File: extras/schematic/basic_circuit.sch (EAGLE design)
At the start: 11 parts, among them M1 ARDUINO-PRO-MINI-3.3V, Y1 32.768kHz

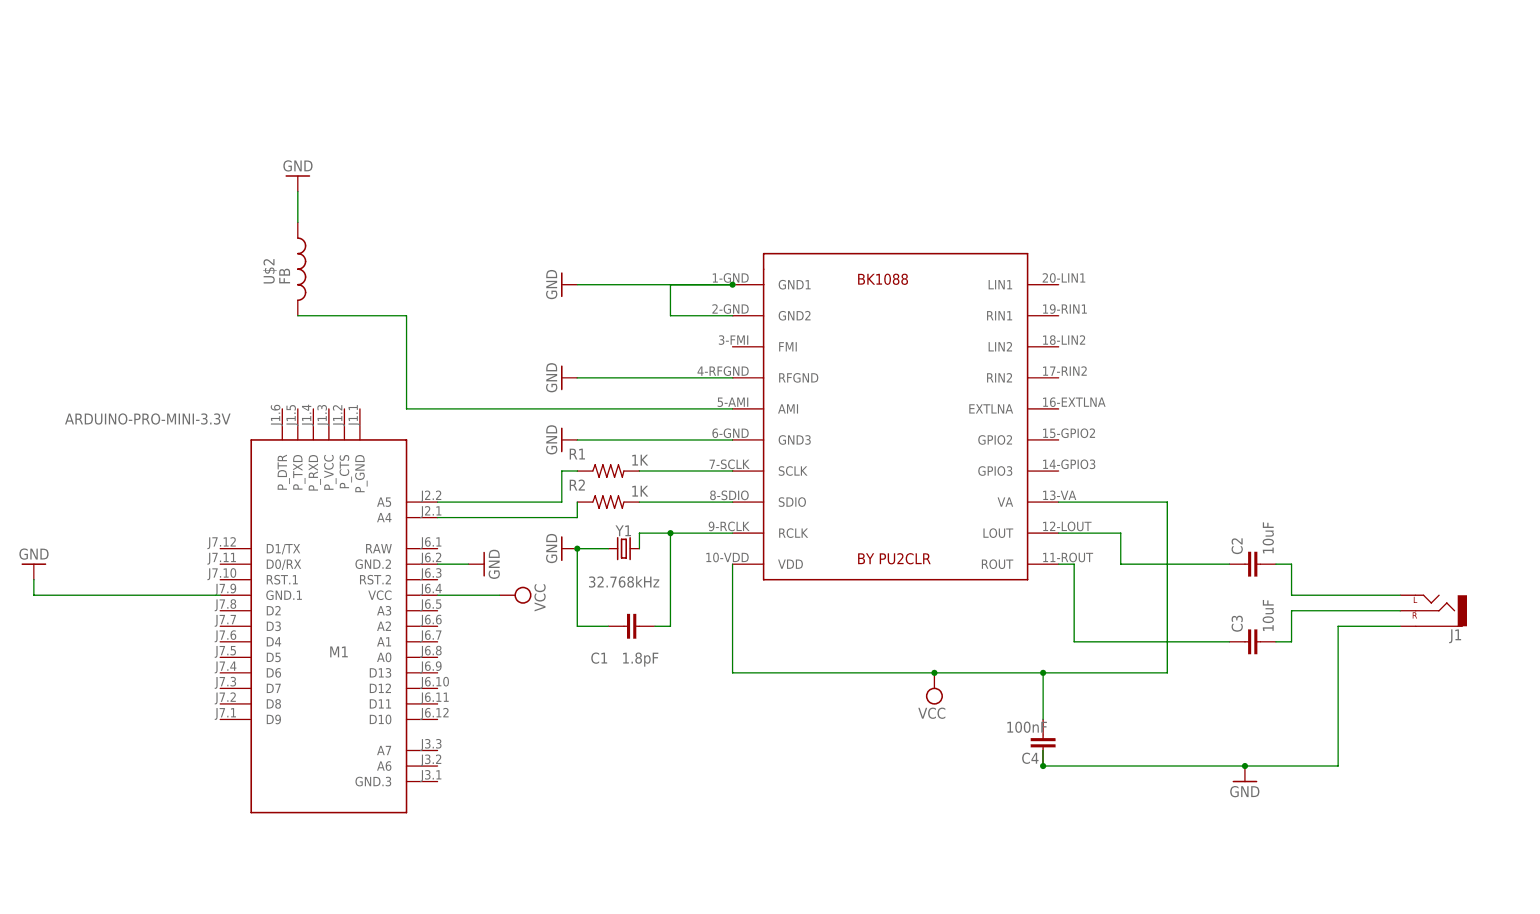
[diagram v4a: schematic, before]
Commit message: BK1088 Arduino Library
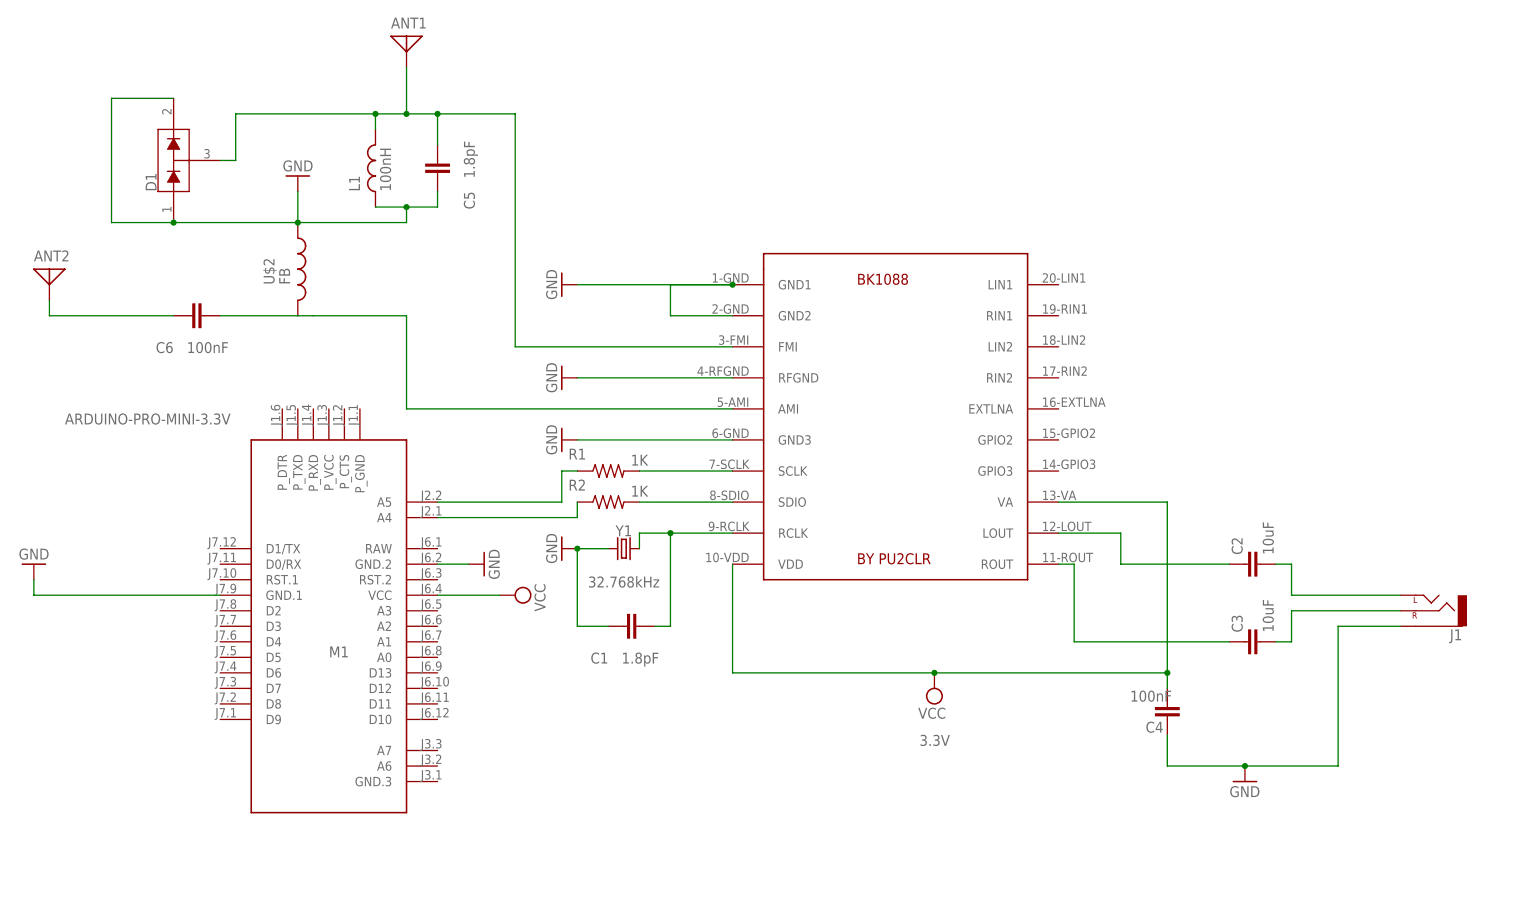
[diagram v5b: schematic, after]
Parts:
- added ANT1, ANT2: (no value), discrete:ANTENNA
- added C5: 1.8pF, capacitor-wima:C5/3
- added C6: 100nF, capacitor-wima:C5/3
- added D1: 200mA/70V, SparkFun-DiscreteSemi:BAV99
- added L1: 100nH, ngspice-simulation:L
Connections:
- new net N$11: ANT2.1, C6.1
- new net N$12: ANT1.1, C5.2, D1.COM, L1.2, U$1.FMI
- net GND: now also C5.1, D1.A1, D1.C2, L1.1
- net N$10: now also C6.2
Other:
- moved on the sheet: C4
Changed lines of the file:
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@@
 <part name="R1" library="Resistor" library_urn="urn:adsk.eagle:library:16378527" deviceset="R-US" device="AXIAL-7.2MM-PITCH" package3d_urn="urn:adsk.eagle:package:16378561/2" technology="_" value="1K"/>
 <part name="R2" library="Resistor" library_urn="urn:adsk.eagle:library:16378527" deviceset="R-US" device="AXIAL-7.2MM-PITCH" package3d_urn="urn:adsk.eagle:package:16378561/2" technology="_" value="1K"/>
-<part name="SUPPLY2" library="supply2" library_urn="urn:adsk.eagle:library:372" deviceset="VCC" device=""/>
+<part name="SUPPLY2" library="supply2" library_urn="urn:adsk.eagle:library:372" deviceset="VCC" device="">
+<attribute name="V" value="3.3V"/>
+</part>
 <part name="GND5" library="supply1" library_urn="urn:adsk.eagle:library:371" deviceset="GND" device=""/>
 <part name="GND4" library="supply1" library_urn="urn:adsk.eagle:library:371" deviceset="GND" device=""/>
@@
 <part name="GND9" library="supply1" library_urn="urn:adsk.eagle:library:371" deviceset="GND" device=""/>
 <part name="C4" library="capacitor-wima" library_urn="urn:adsk.eagle:library:116" deviceset="C" device="5/3" package3d_urn="urn:adsk.eagle:package:5433/1" value="100nF"/>
+<part name="L1" library="ngspice-simulation" library_urn="urn:adsk.eagle:library:527439" deviceset="L" device="" value="100nH"/>
+<part name="C5" library="capacitor-wima" library_urn="urn:adsk.eagle:library:116" deviceset="C" device="5/3" package3d_urn="urn:adsk.eagle:package:5433/1" value="1.8pF"/>
+<part name="ANT1" library="discrete" library_urn="urn:adsk.eagle:library:211" deviceset="ANTENNA" device="" package3d_urn="urn:adsk.eagle:package:12928/1"/>
+<part name="D1" library="SparkFun-DiscreteSemi" library_urn="urn:adsk.eagle:library:514" deviceset="BAV99" device="" package3d_urn="urn:adsk.eagle:package:38446/1" value="200mA/70V"/>
+<part name="C6" library="capacitor-wima" library_urn="urn:adsk.eagle:library:116" deviceset="C" device="5/3" package3d_urn="urn:adsk.eagle:package:5433/1" value="100nF"/>
+<part name="ANT2" library="discrete" library_urn="urn:adsk.eagle:library:211" deviceset="ANTENNA" device="" package3d_urn="urn:adsk.eagle:package:12928/1"/>
 </parts>
 <sheets>
@@
 <instance part="SUPPLY2" gate="G$1" x="81.28" y="10.16" smashed="yes" rot="R180">
 <attribute name="VALUE" x="83.185" y="6.985" size="1.778" layer="96" rot="R180"/>
+<attribute name="V" x="83.82" y="2.54" size="1.778" layer="96" rot="R180"/>
 </instance>
 <instance part="GND5" gate="1" x="-66.04" y="30.48" smashed="yes" rot="R180">
@@
 <attribute name="VALUE" x="129.54" y="-7.62" size="1.778" layer="96"/>
 </instance>
-<instance part="C4" gate="G$1" x="99.06" y="2.54" smashed="yes">
-<attribute name="NAME" x="95.504" y="-2.159" size="1.778" layer="95"/>
-<attribute name="VALUE" x="92.964" y="2.921" size="1.778" layer="96"/>
+<instance part="C4" gate="G$1" x="119.38" y="7.62" smashed="yes">
+<attribute name="NAME" x="115.824" y="2.921" size="1.778" layer="95"/>
+<attribute name="VALUE" x="113.284" y="8.001" size="1.778" layer="96"/>
+</instance>
+<instance part="L1" gate="G$1" x="-10.16" y="93.98" smashed="yes" rot="R90">
+<attribute name="NAME" x="-12.7" y="91.44" size="1.778" layer="95" rot="R90"/>
+<attribute name="VALUE" x="-7.62" y="91.44" size="1.778" layer="96" rot="R90"/>
+</instance>
+<instance part="C5" gate="G$1" x="0" y="93.98" smashed="yes" rot="R180">
+<attribute name="NAME" x="6.096" y="88.519" size="1.778" layer="95" rot="R90"/>
+<attribute name="VALUE" x="6.096" y="93.599" size="1.778" layer="96" rot="R90"/>
+</instance>
+<instance part="ANT1" gate="A" x="-5.08" y="116.84" smashed="yes">
+<attribute name="NAME" x="-7.62" y="118.11" size="1.778" layer="95"/>
+<attribute name="VALUE" x="-2.54" y="111.76" size="1.778" layer="96"/>
+</instance>
+<instance part="D1" gate="G$1" x="-43.18" y="96.52" smashed="yes" rot="R90">
+<attribute name="NAME" x="-45.974" y="91.44" size="1.778" layer="95" font="vector" rot="R90"/>
+<attribute name="VALUE" x="-40.386" y="96.774" size="1.778" layer="96" font="vector" rot="R90" align="top-left" display="off"/>
+</instance>
+<instance part="C6" gate="G$1" x="-40.64" y="71.12" smashed="yes" rot="R90">
+<attribute name="NAME" x="-46.101" y="65.024" size="1.778" layer="95"/>
+<attribute name="VALUE" x="-41.021" y="65.024" size="1.778" layer="96"/>
+</instance>
+<instance part="ANT2" gate="A" x="-63.5" y="78.74" smashed="yes">
+<attribute name="NAME" x="-66.04" y="80.01" size="1.778" layer="95"/>
+<attribute name="VALUE" x="-60.96" y="73.66" size="1.778" layer="96"/>
 </instance>
 </instances>
@@
 <pinref part="GND8" gate="1" pin="GND"/>
 <wire x1="-22.86" y1="86.36" x2="-22.86" y2="91.44" width="0.1524" layer="91"/>
+<wire x1="-22.86" y1="86.36" x2="-5.08" y2="86.36" width="0.1524" layer="91"/>
+<junction x="-22.86" y="86.36"/>
+<pinref part="L1" gate="G$1" pin="1"/>
+<wire x1="-10.16" y1="88.9" x2="-5.08" y2="88.9" width="0.1524" layer="91"/>
+<pinref part="C5" gate="G$1" pin="1"/>
+<wire x1="-5.08" y1="88.9" x2="0" y2="88.9" width="0.1524" layer="91"/>
+<wire x1="0" y1="88.9" x2="0" y2="91.44" width="0.1524" layer="91"/>
+<wire x1="-5.08" y1="86.36" x2="-5.08" y2="88.9" width="0.1524" layer="91"/>
+<junction x="-5.08" y="88.9"/>
+<pinref part="D1" gate="G$1" pin="C2"/>
+<wire x1="-43.18" y1="106.68" x2="-53.34" y2="106.68" width="0.1524" layer="91"/>
+<wire x1="-53.34" y1="106.68" x2="-53.34" y2="86.36" width="0.1524" layer="91"/>
+<pinref part="D1" gate="G$1" pin="A1"/>
+<wire x1="-53.34" y1="86.36" x2="-43.18" y2="86.36" width="0.1524" layer="91"/>
+<wire x1="-43.18" y1="86.36" x2="-22.86" y2="86.36" width="0.1524" layer="91"/>
+<junction x="-43.18" y="86.36"/>
 </segment>
 <segment>
@@
 <wire x1="147.32" y1="-2.54" x2="132.08" y2="-2.54" width="0.1524" layer="91"/>
 <pinref part="C4" gate="G$1" pin="2"/>
-<wire x1="99.06" y1="-2.54" x2="132.08" y2="-2.54" width="0.1524" layer="91"/>
+<wire x1="119.38" y1="2.54" x2="119.38" y2="-2.54" width="0.1524" layer="91"/>
+<wire x1="119.38" y1="-2.54" x2="132.08" y2="-2.54" width="0.1524" layer="91"/>
 <junction x="132.08" y="-2.54"/>
-<wire x1="99.06" y1="-2.54" x2="99.06" y2="0" width="0.1524" layer="91"/>
-<junction x="99.06" y="-2.54"/>
 </segment>
 </net>
@@
 <wire x1="101.6" y1="40.64" x2="119.38" y2="40.64" width="0.1524" layer="91"/>
 <wire x1="119.38" y1="40.64" x2="119.38" y2="12.7" width="0.1524" layer="91"/>
-<wire x1="119.38" y1="12.7" x2="99.06" y2="12.7" width="0.1524" layer="91"/>
+<wire x1="119.38" y1="12.7" x2="81.28" y2="12.7" width="0.1524" layer="91"/>
 <junction x="81.28" y="12.7"/>
 <pinref part="C4" gate="G$1" pin="1"/>
-<wire x1="99.06" y1="12.7" x2="81.28" y2="12.7" width="0.1524" layer="91"/>
-<wire x1="99.06" y1="5.08" x2="99.06" y2="12.7" width="0.1524" layer="91"/>
-<junction x="99.06" y="12.7"/>
+<wire x1="119.38" y1="10.16" x2="119.38" y2="12.7" width="0.1524" layer="91"/>
+<junction x="119.38" y="12.7"/>
 </segment>
 </net>
@@
 <wire x1="-5.08" y1="55.88" x2="-5.08" y2="71.12" width="0.1524" layer="91"/>
 <pinref part="U$2" gate="G$1" pin="2"/>
-<wire x1="-5.08" y1="71.12" x2="-22.86" y2="71.12" width="0.1524" layer="91"/>
-</segment>
-</net>
+<wire x1="-5.08" y1="71.12" x2="-20.32" y2="71.12" width="0.1524" layer="91"/>
+<pinref part="C6" gate="G$1" pin="2"/>
+<wire x1="-20.32" y1="71.12" x2="-22.86" y2="71.12" width="0.1524" layer="91"/>
+<wire x1="-35.56" y1="71.12" x2="-22.86" y2="71.12" width="0.1524" layer="91"/>
+</segment>
+</net>
+<net name="N$12" class="0">
+<segment>
+<pinref part="L1" gate="G$1" pin="2"/>
+<wire x1="-10.16" y1="101.6" x2="-10.16" y2="104.14" width="0.1524" layer="91"/>
+<wire x1="-10.16" y1="104.14" x2="-5.08" y2="104.14" width="0.1524" layer="91"/>
+<pinref part="C5" gate="G$1" pin="2"/>
+<wire x1="-5.08" y1="104.14" x2="0" y2="104.14" width="0.1524" layer="91"/>
+<wire x1="0" y1="104.14" x2="0" y2="99.06" width="0.1524" layer="91"/>
+<pinref part="ANT1" gate="A" pin="1"/>
+<wire x1="-5.08" y1="111.76" x2="-5.08" y2="104.14" width="0.1524" layer="91"/>
+<junction x="-5.08" y="104.14"/>
+<pinref part="U$1" gate="G$1" pin="FMI"/>
+<wire x1="48.26" y1="66.04" x2="12.7" y2="66.04" width="0.1524" layer="91"/>
+<wire x1="12.7" y1="66.04" x2="12.7" y2="104.14" width="0.1524" layer="91"/>
+<wire x1="12.7" y1="104.14" x2="0" y2="104.14" width="0.1524" layer="91"/>
+<junction x="0" y="104.14"/>
+<pinref part="D1" gate="G$1" pin="COM"/>
+<wire x1="-35.56" y1="96.52" x2="-33.02" y2="96.52" width="0.1524" layer="91"/>
+<wire x1="-33.02" y1="96.52" x2="-33.02" y2="104.14" width="0.1524" layer="91"/>
+<wire x1="-33.02" y1="104.14" x2="-10.16" y2="104.14" width="0.1524" layer="91"/>
+<junction x="-10.16" y="104.14"/>
+</segment>
+</net>
+<net name="N$11" class="0">
+<segment>
+<pinref part="ANT2" gate="A" pin="1"/>
+<pinref part="C6" gate="G$1" pin="1"/>
+<wire x1="-63.5" y1="73.66" x2="-63.5" y2="71.12" width="0.1524" layer="91"/>
+<wire x1="-63.5" y1="71.12" x2="-43.18" y2="71.12" width="0.1524" layer="91"/>
+</segment>
+</net>

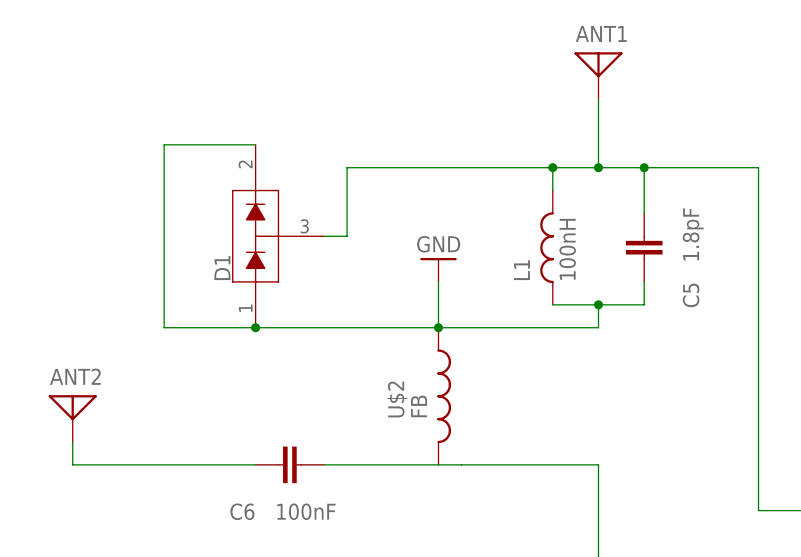
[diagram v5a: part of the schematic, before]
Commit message: BK1088 Arduino Library
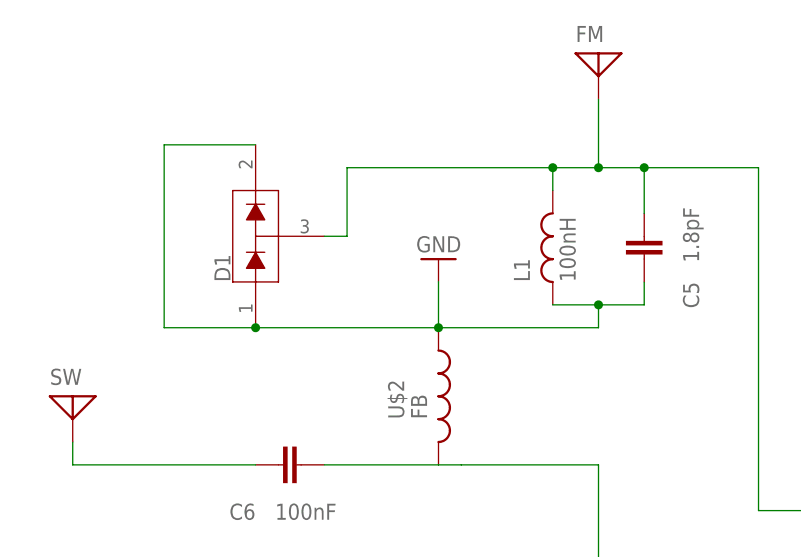
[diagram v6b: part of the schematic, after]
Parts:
- renumbered ANT1 to FM, ANT2 to SW
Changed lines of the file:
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@@
 <part name="L1" library="ngspice-simulation" library_urn="urn:adsk.eagle:library:527439" deviceset="L" device="" value="100nH"/>
 <part name="C5" library="capacitor-wima" library_urn="urn:adsk.eagle:library:116" deviceset="C" device="5/3" package3d_urn="urn:adsk.eagle:package:5433/1" value="1.8pF"/>
-<part name="ANT1" library="discrete" library_urn="urn:adsk.eagle:library:211" deviceset="ANTENNA" device="" package3d_urn="urn:adsk.eagle:package:12928/1"/>
+<part name="FM" library="discrete" library_urn="urn:adsk.eagle:library:211" deviceset="ANTENNA" device="" package3d_urn="urn:adsk.eagle:package:12928/1"/>
 <part name="D1" library="SparkFun-DiscreteSemi" library_urn="urn:adsk.eagle:library:514" deviceset="BAV99" device="" package3d_urn="urn:adsk.eagle:package:38446/1" value="200mA/70V"/>
 <part name="C6" library="capacitor-wima" library_urn="urn:adsk.eagle:library:116" deviceset="C" device="5/3" package3d_urn="urn:adsk.eagle:package:5433/1" value="100nF"/>
-<part name="ANT2" library="discrete" library_urn="urn:adsk.eagle:library:211" deviceset="ANTENNA" device="" package3d_urn="urn:adsk.eagle:package:12928/1"/>
+<part name="SW" library="discrete" library_urn="urn:adsk.eagle:library:211" deviceset="ANTENNA" device="" package3d_urn="urn:adsk.eagle:package:12928/1"/>
 </parts>
 <sheets>
@@
 <attribute name="VALUE" x="6.096" y="93.599" size="1.778" layer="96" rot="R90"/>
 </instance>
-<instance part="ANT1" gate="A" x="-5.08" y="116.84" smashed="yes">
+<instance part="FM" gate="A" x="-5.08" y="116.84" smashed="yes">
 <attribute name="NAME" x="-7.62" y="118.11" size="1.778" layer="95"/>
 <attribute name="VALUE" x="-2.54" y="111.76" size="1.778" layer="96"/>
@@
 <attribute name="VALUE" x="-41.021" y="65.024" size="1.778" layer="96"/>
 </instance>
-<instance part="ANT2" gate="A" x="-63.5" y="78.74" smashed="yes">
+<instance part="SW" gate="A" x="-63.5" y="78.74" smashed="yes">
 <attribute name="NAME" x="-66.04" y="80.01" size="1.778" layer="95"/>
 <attribute name="VALUE" x="-60.96" y="73.66" size="1.778" layer="96"/>
@@
 <wire x1="-5.08" y1="104.14" x2="0" y2="104.14" width="0.1524" layer="91"/>
 <wire x1="0" y1="104.14" x2="0" y2="99.06" width="0.1524" layer="91"/>
-<pinref part="ANT1" gate="A" pin="1"/>
+<pinref part="FM" gate="A" pin="1"/>
 <wire x1="-5.08" y1="111.76" x2="-5.08" y2="104.14" width="0.1524" layer="91"/>
 <junction x="-5.08" y="104.14"/>
@@
 <net name="N$11" class="0">
 <segment>
-<pinref part="ANT2" gate="A" pin="1"/>
+<pinref part="SW" gate="A" pin="1"/>
 <pinref part="C6" gate="G$1" pin="1"/>
 <wire x1="-63.5" y1="73.66" x2="-63.5" y2="71.12" width="0.1524" layer="91"/>

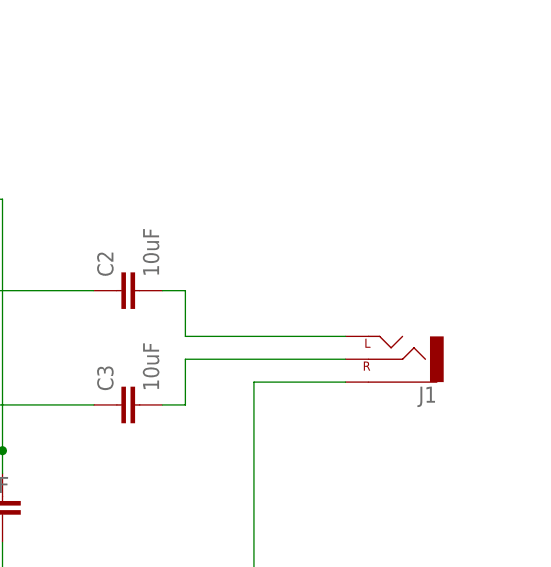
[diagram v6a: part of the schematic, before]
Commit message: BK108X Arduino Library
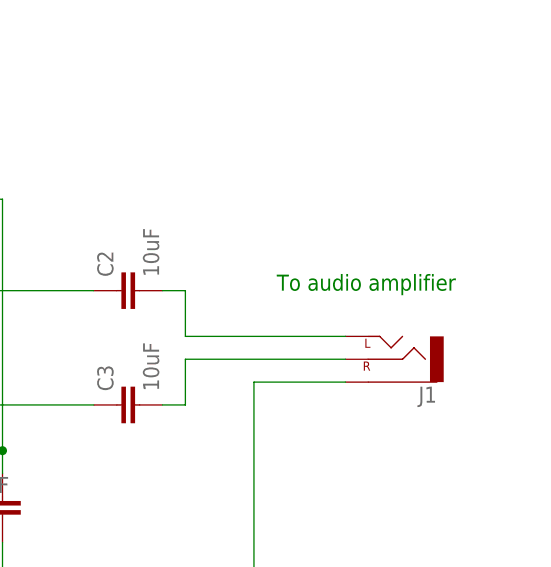
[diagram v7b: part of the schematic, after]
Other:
- note added: "To audio amplifier"
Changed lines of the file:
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@@
 <sheet>
 <plain>
+<text x="149.86" y="30.48" size="1.778" layer="91">To audio amplifier</text>
 </plain>
 <instances>
